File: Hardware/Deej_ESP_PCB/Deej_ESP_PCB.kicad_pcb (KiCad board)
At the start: 2 copper layers, 0 parts

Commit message: Started PCB Layout Added Mounting Holes and Knobs
- Started doing PCB layout. I have an idea of large component placement
  and therefore overall board size but still working out finalizing
  them.
- Added platted mounting holes to the board mostly for support since
  most of this board is user interfaces I expect there to be a good
  amount of force applied to the sliders, buttons, and knobs.
- Found some metal knobs for the rotary potentiometers and added them to
  the custom BOM.
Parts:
- added C1: 0.1uF, Capacitor_SMD:C_0603_1608Metric_Pad1.08x0.95mm_HandSolder, F.Cu at (-170.9, 104.7)
- added C10: 0.1uF, Capacitor_SMD:C_0603_1608Metric_Pad1.08x0.95mm_HandSolder, F.Cu at (-170.9, 112.2)
- added C11: 0.1uF, Capacitor_SMD:C_0603_1608Metric_Pad1.08x0.95mm_HandSolder, F.Cu at (-170.9, 114.7)
- added C12: 0.1uF, Capacitor_SMD:C_0603_1608Metric_Pad1.08x0.95mm_HandSolder, F.Cu at (-170.9, 117.2)
- added C13: 0.1uF, Capacitor_SMD:C_0603_1608Metric_Pad1.08x0.95mm_HandSolder, F.Cu at (-170.9, 119.7)
- added C14: 0.1uF, Capacitor_SMD:C_0603_1608Metric_Pad1.08x0.95mm_HandSolder, F.Cu at (-170.9, 122.2)
- added C15: 0.1uF, Capacitor_SMD:C_0603_1608Metric_Pad1.08x0.95mm_HandSolder, F.Cu at (-170.9, 124.7)
- added C16: 10uF, Capacitor_SMD:C_0603_1608Metric_Pad1.08x0.95mm_HandSolder, F.Cu at (-170.9, 127.2)
- added C17: 0.1uF, Capacitor_Tantalum_SMD:CP_EIA-3216-18_Kemet-A_HandSolder, F.Cu at (-123.7, 105.0)
- added C18: 0.1uF, Capacitor_Tantalum_SMD:CP_EIA-3216-18_Kemet-A_HandSolder, F.Cu at (-123.7, 108.1)
- added C19: 0.1uF, Capacitor_Tantalum_SMD:CP_EIA-3216-18_Kemet-A_HandSolder, F.Cu at (-123.7, 111.3)
- added C2: 0.1uF, Capacitor_SMD:C_0603_1608Metric_Pad1.08x0.95mm_HandSolder, F.Cu at (-170.9, 107.2)
- added C20: 0.1uF, Capacitor_Tantalum_SMD:CP_EIA-3216-18_Kemet-A_HandSolder, F.Cu at (-123.7, 114.4)
- added C21: 0.1uF, Capacitor_SMD:C_0603_1608Metric_Pad1.08x0.95mm_HandSolder, F.Cu at (-170.9, 129.8)
- added C22: 0.1uF, Capacitor_SMD:C_0603_1608Metric_Pad1.08x0.95mm_HandSolder, F.Cu at (-166.5, 104.7)
- added C23: 10uF, Capacitor_SMD:C_0603_1608Metric_Pad1.08x0.95mm_HandSolder, F.Cu at (-166.5, 107.2)
- added C24: 0.1uF, Capacitor_SMD:C_0603_1608Metric_Pad1.08x0.95mm_HandSolder, F.Cu at (-166.5, 109.7)
- added C25: 0.1uF, Capacitor_SMD:C_0603_1608Metric_Pad1.08x0.95mm_HandSolder, F.Cu at (-166.5, 112.2)
- added C26: 0.1uF, Capacitor_SMD:C_0603_1608Metric_Pad1.08x0.95mm_HandSolder, F.Cu at (-166.5, 114.7)
- added C27: 0.1uF, Capacitor_SMD:C_0603_1608Metric_Pad1.08x0.95mm_HandSolder, F.Cu at (-166.5, 117.2)
- added C28: 0.1uF, Capacitor_SMD:C_0603_1608Metric_Pad1.08x0.95mm_HandSolder, F.Cu at (-166.5, 119.7)
- added C29: 0.1uF, Capacitor_SMD:C_0603_1608Metric_Pad1.08x0.95mm_HandSolder, F.Cu at (-166.5, 122.2)
- added C3: 0.1uF, Capacitor_Tantalum_SMD:CP_EIA-3216-18_Kemet-A_HandSolder, F.Cu at (-129.7, 105.0)
- added C30: 1uF, Capacitor_SMD:C_0603_1608Metric_Pad1.08x0.95mm_HandSolder, F.Cu at (-166.5, 124.7)
- added C31: 0.1uF, Capacitor_Tantalum_SMD:CP_EIA-3216-18_Kemet-A_HandSolder, F.Cu at (-123.7, 117.6)
- added C32: 0.1uF, Capacitor_Tantalum_SMD:CP_EIA-3216-18_Kemet-A_HandSolder, F.Cu at (-123.7, 120.7)
- added C33: 0.1uF, Capacitor_Tantalum_SMD:CP_EIA-3216-18_Kemet-A_HandSolder, F.Cu at (-117.6, 105.0)
- added C34: 0.1uF, Capacitor_Tantalum_SMD:CP_EIA-3216-18_Kemet-A_HandSolder, F.Cu at (-117.6, 108.1)
- added C35: 0.1uF, Capacitor_Tantalum_SMD:CP_EIA-3216-18_Kemet-A_HandSolder, F.Cu at (-117.6, 111.3)
- added C36: 0.1uF, Capacitor_Tantalum_SMD:CP_EIA-3216-18_Kemet-A_HandSolder, F.Cu at (-117.6, 114.4)
- added C37: 22uF, Capacitor_SMD:C_0603_1608Metric_Pad1.08x0.95mm_HandSolder, F.Cu at (-166.5, 127.2)
- added C38: 0.1uF, Capacitor_SMD:C_0603_1608Metric_Pad1.08x0.95mm_HandSolder, F.Cu at (-166.5, 129.8)
- added C4: 0.1uF, Capacitor_Tantalum_SMD:CP_EIA-3216-18_Kemet-A_HandSolder, F.Cu at (-129.7, 108.1)
- added C5: 0.1uF, Capacitor_Tantalum_SMD:CP_EIA-3216-18_Kemet-A_HandSolder, F.Cu at (-129.7, 111.3)
- added C6: 0.1uF, Capacitor_Tantalum_SMD:CP_EIA-3216-18_Kemet-A_HandSolder, F.Cu at (-129.7, 114.4)
- added C7: 0.1uF, Capacitor_Tantalum_SMD:CP_EIA-3216-18_Kemet-A_HandSolder, F.Cu at (-129.7, 117.6)
- added C8: 0.1uF, Capacitor_Tantalum_SMD:CP_EIA-3216-18_Kemet-A_HandSolder, F.Cu at (-129.7, 120.7)
- added C9: 0.1uF, Capacitor_SMD:C_0603_1608Metric_Pad1.08x0.95mm_HandSolder, F.Cu at (-170.9, 109.7)
- added CR1: ESDALC6V1-1U2, STM:DIODE_ESDALC6V1-1U2_STM, F.Cu at (-111.8, 47.1)
- added CR10: ESDALC6V1-1U2, STM:DIODE_ESDALC6V1-1U2_STM, F.Cu at (-107.1, 47.1)
- added CR11: ESDALC6V1-1U2, STM:DIODE_ESDALC6V1-1U2_STM, F.Cu at (-107.1, 49.1)
- added CR12: ESDALC6V1-1U2, STM:DIODE_ESDALC6V1-1U2_STM, F.Cu at (-107.1, 51.2)
- added CR13: ESDALC6V1-1U2, STM:DIODE_ESDALC6V1-1U2_STM, F.Cu at (-107.1, 53.2)
- added CR14: ESDALC6V1-1U2, STM:DIODE_ESDALC6V1-1U2_STM, F.Cu at (-104.8, 47.1)
- added CR15: ESDALC6V1-1U2, STM:DIODE_ESDALC6V1-1U2_STM, F.Cu at (-104.8, 49.1)
- added CR16: ESDALC6V1-1U2, STM:DIODE_ESDALC6V1-1U2_STM, F.Cu at (-104.8, 51.2)
- added CR17: ESDALC6V1-1U2, STM:DIODE_ESDALC6V1-1U2_STM, F.Cu at (-104.8, 53.2)
- added CR2: ESDALC6V1-1U2, STM:DIODE_ESDALC6V1-1U2_STM, F.Cu at (-111.8, 49.1)
- added CR3: ESDALC6V1-1U2, STM:DIODE_ESDALC6V1-1U2_STM, F.Cu at (-111.8, 51.2)
- added CR4: ESDALC6V1-1U2, STM:DIODE_ESDALC6V1-1U2_STM, F.Cu at (-111.8, 53.2)
- added CR5: ESDALC6V1-1U2, STM:DIODE_ESDALC6V1-1U2_STM, F.Cu at (-109.5, 47.1)
- added CR6: ESDALC6V1-1U2, STM:DIODE_ESDALC6V1-1U2_STM, F.Cu at (-109.5, 49.1)
- added CR7: ESDA25P35-1U1M, STM:QFN1610_STM, F.Cu at (-101.3, 67.7)
- added CR8: ESDALC6V1-1U2, STM:DIODE_ESDALC6V1-1U2_STM, F.Cu at (-109.5, 51.2)
- added CR9: ESDALC6V1-1U2, STM:DIODE_ESDALC6V1-1U2_STM, F.Cu at (-109.5, 53.2)
- added D1: Inolux_IN-PI554FCH, LED_SMD:LED_Inolux_IN-PI554FCH_PLCC4_5.0x5.0mm_P3.2mm, F.Cu at (284.6, 151.7)
- added D10: Inolux_IN-PI554FCH, LED_SMD:LED_Inolux_IN-PI554FCH_PLCC4_5.0x5.0mm_P3.2mm, F.Cu at (148.0, 217.5)
- added D11: Inolux_IN-PI554FCH, LED_SMD:LED_Inolux_IN-PI554FCH_PLCC4_5.0x5.0mm_P3.2mm, F.Cu at (155.5, 217.5)
- added D12: Inolux_IN-PI554FCH, LED_SMD:LED_Inolux_IN-PI554FCH_PLCC4_5.0x5.0mm_P3.2mm, F.Cu at (174.5, 217.5)
- added D13: Red LED, LED_SMD:LED_0603_1608Metric_Pad1.05x0.95mm_HandSolder, F.Cu at (-100.3, 55.5)
- added D14: Inolux_IN-PI554FCH, LED_SMD:LED_Inolux_IN-PI554FCH_PLCC4_5.0x5.0mm_P3.2mm, F.Cu at (182.0, 217.5)
- added D15: Inolux_IN-PI554FCH, LED_SMD:LED_Inolux_IN-PI554FCH_PLCC4_5.0x5.0mm_P3.2mm, F.Cu at (201.0, 217.5)
- added D16: Inolux_IN-PI554FCH, LED_SMD:LED_Inolux_IN-PI554FCH_PLCC4_5.0x5.0mm_P3.2mm, F.Cu at (208.5, 217.5)
- added D17: Inolux_IN-PI554FCH, LED_SMD:LED_Inolux_IN-PI554FCH_PLCC4_5.0x5.0mm_P3.2mm, F.Cu at (227.5, 217.5)
- added D18: MMSD4148T1G, Diode_SMD:D_SOD-123, F.Cu at (-110.0, 69.3)
- added D19: MMSD4148T1G, Diode_SMD:D_SOD-123, F.Cu at (-110.0, 72.6)
- added D2: Inolux_IN-PI554FCH, LED_SMD:LED_Inolux_IN-PI554FCH_PLCC4_5.0x5.0mm_P3.2mm, F.Cu at (284.6, 232.0)
- added D20: MMSD4148T1G, Diode_SMD:D_SOD-123, F.Cu at (-110.0, 76.0)
- added D21: MMSD4148T1G, Diode_SMD:D_SOD-123, F.Cu at (-110.0, 79.3)
- added D22: Orange LED, LED_SMD:LED_0603_1608Metric_Pad1.05x0.95mm_HandSolder, F.Cu at (-100.3, 58.1)
- added D23: Inolux_IN-PI554FCH, LED_SMD:LED_Inolux_IN-PI554FCH_PLCC4_5.0x5.0mm_P3.2mm, F.Cu at (235.0, 217.5)
- added D24: Inolux_IN-PI554FCH, LED_SMD:LED_Inolux_IN-PI554FCH_PLCC4_5.0x5.0mm_P3.2mm, F.Cu at (254.0, 217.5)
- added D25: Orange LED, LED_SMD:LED_0603_1608Metric_Pad1.05x0.95mm_HandSolder, F.Cu at (-100.3, 60.7)
- added D26: Green LED, LED_SMD:LED_0603_1608Metric_Pad1.05x0.95mm_HandSolder, F.Cu at (-100.3, 63.2)
- added D3: Inolux_IN-PI554FCH, LED_SMD:LED_Inolux_IN-PI554FCH_PLCC4_5.0x5.0mm_P3.2mm, F.Cu at (102.5, 217.5)
- added D4: Inolux_IN-PI554FCH, LED_SMD:LED_Inolux_IN-PI554FCH_PLCC4_5.0x5.0mm_P3.2mm, F.Cu at (121.5, 217.5)
- added D5: MMSD4148T1G, Diode_SMD:D_SOD-123, F.Cu at (-110.0, 55.9)
- added D6: MMSD4148T1G, Diode_SMD:D_SOD-123, F.Cu at (-110.0, 59.2)
- added D7: MMSD4148T1G, Diode_SMD:D_SOD-123, F.Cu at (-110.0, 62.6)
- added D8: MMSD4148T1G, Diode_SMD:D_SOD-123, F.Cu at (-110.0, 65.9)
- added D9: Inolux_IN-PI554FCH, LED_SMD:LED_Inolux_IN-PI554FCH_PLCC4_5.0x5.0mm_P3.2mm, F.Cu at (129.0, 217.5)
- added H1: ~, MountingHole:MountingHole_3.2mm_M3_Pad, F.Cu at (101.0, 62.5)
- added H10: MountingHole_Pad, MountingHole:MountingHole_3.2mm_M3_Pad, F.Cu at (125.5, 155.0)
- added H11: MountingHole_Pad, MountingHole:MountingHole_3.2mm_M3_Pad, F.Cu at (178.5, 155.0)
- added H12: MountingHole_Pad, MountingHole:MountingHole_3.2mm_M3_Pad, F.Cu at (231.5, 155.0)
- added H2: ~, MountingHole:MountingHole_3.2mm_M3_Pad, F.Cu at (101.0, 238.0)
- added H3: ~, MountingHole:MountingHole_3.2mm_M3_Pad, F.Cu at (151.5, 238.0)
- added H4: ~, MountingHole:MountingHole_3.2mm_M3_Pad, F.Cu at (204.5, 238.0)
- added H5: ~, MountingHole:MountingHole_3.2mm_M3_Pad, F.Cu at (257.5, 238.0)
- added H6: MountingHole_Pad, MountingHole:MountingHole_3.2mm_M3_Pad, F.Cu at (299.0, 238.0)
- added H7: MountingHole_Pad, MountingHole:MountingHole_3.2mm_M3_Pad, F.Cu at (299.0, 157.0)
- added H8: MountingHole_Pad, MountingHole:MountingHole_3.2mm_M3_Pad, F.Cu at (299.0, 62.5)
- added H9: MountingHole_Pad, MountingHole:MountingHole_3.2mm_M3_Pad, F.Cu at (190.0, 62.5)
- added J1: USB_C_Receptacle_USB2.0_16P, Connector_USB:USB_C_Receptacle_GCT_USB4085, F.Cu at (182.0, 64.5)
- added J2: UART Header, Connector_PinHeader_2.54mm:PinHeader_1x04_P2.54mm_Vertical, F.Cu at (262.3, 91.5)
- added P1: 10K, Bourns_Potentiometer:PTL0115R0103B1, F.Cu at (113.2, 93.5)
- added P2: 10K, Bourns_Potentiometer:PTL0115R0103B1, F.Cu at (139.8, 93.5)
- added P3: 10K, Bourns_Potentiometer:PTL0115R0103B1, F.Cu at (166.2, 93.5)
- added P4: 10K, Bourns_Potentiometer:PTL0115R0103B1, F.Cu at (192.8, 93.5)
- added P5: 10K, Bourns_Potentiometer:PTL0115R0103B1, F.Cu at (219.2, 93.5)
- added P6: 10K, Bourns_Potentiometer:PTL0115R0103B1, F.Cu at (245.8, 93.5)
- added R1: 499, Capacitor_SMD:C_0603_1608Metric_Pad1.08x0.95mm_HandSolder, F.Cu at (-162.2, 104.7)
- added R10: 5.1K, Capacitor_SMD:C_0603_1608Metric_Pad1.08x0.95mm_HandSolder, F.Cu at (-162.2, 127.2)
- added R11: 5.1K, Capacitor_SMD:C_0603_1608Metric_Pad1.08x0.95mm_HandSolder, F.Cu at (-162.2, 129.8)
- added R12: 200, Capacitor_SMD:C_0603_1608Metric_Pad1.08x0.95mm_HandSolder, F.Cu at (-157.8, 104.7)
- added R13: 1K, Capacitor_SMD:C_0603_1608Metric_Pad1.08x0.95mm_HandSolder, F.Cu at (-157.8, 107.2)
- added R14: 1K, Capacitor_SMD:C_0603_1608Metric_Pad1.08x0.95mm_HandSolder, F.Cu at (-157.8, 109.7)
- added R15: 1K, Capacitor_SMD:C_0603_1608Metric_Pad1.08x0.95mm_HandSolder, F.Cu at (-157.8, 112.2)
- added R16: 1K, Capacitor_SMD:C_0603_1608Metric_Pad1.08x0.95mm_HandSolder, F.Cu at (-157.8, 114.7)
- added R17: 10K, Capacitor_SMD:C_0603_1608Metric_Pad1.08x0.95mm_HandSolder, F.Cu at (-157.8, 117.2)
- added R18: 10K, Capacitor_SMD:C_0603_1608Metric_Pad1.08x0.95mm_HandSolder, F.Cu at (-157.8, 119.7)
- added R19: 10K, Capacitor_SMD:C_0603_1608Metric_Pad1.08x0.95mm_HandSolder, F.Cu at (-157.8, 122.2)
- added R2: 1K, Capacitor_SMD:C_0603_1608Metric_Pad1.08x0.95mm_HandSolder, F.Cu at (-162.2, 107.2)
- added R20: 10K, Capacitor_SMD:C_0603_1608Metric_Pad1.08x0.95mm_HandSolder, F.Cu at (-157.8, 124.7)
- added R21: 100, Capacitor_SMD:C_0603_1608Metric_Pad1.08x0.95mm_HandSolder, F.Cu at (-157.8, 127.2)
- added R23: 100, Capacitor_SMD:C_0603_1608Metric_Pad1.08x0.95mm_HandSolder, F.Cu at (-157.8, 129.8)
- added R24: 10, Capacitor_SMD:C_0603_1608Metric_Pad1.08x0.95mm_HandSolder, F.Cu at (-153.5, 104.7)
- added R25: 10K, Capacitor_SMD:C_0603_1608Metric_Pad1.08x0.95mm_HandSolder, F.Cu at (-153.5, 107.2)
- added R26: 100, Capacitor_SMD:C_0603_1608Metric_Pad1.08x0.95mm_HandSolder, F.Cu at (-153.5, 109.7)
- added R27: 100, Capacitor_SMD:C_0603_1608Metric_Pad1.08x0.95mm_HandSolder, F.Cu at (-153.5, 112.2)
- added R28: 100, Capacitor_SMD:C_0603_1608Metric_Pad1.08x0.95mm_HandSolder, F.Cu at (-153.5, 114.7)
- added R29: 100, Capacitor_SMD:C_0603_1608Metric_Pad1.08x0.95mm_HandSolder, F.Cu at (-153.5, 117.2)
- added R3: 1K, Capacitor_SMD:C_0603_1608Metric_Pad1.08x0.95mm_HandSolder, F.Cu at (-162.2, 109.7)
- added R30: 100, Capacitor_SMD:C_0603_1608Metric_Pad1.08x0.95mm_HandSolder, F.Cu at (-153.5, 119.7)
- added R31: 100, Capacitor_SMD:C_0603_1608Metric_Pad1.08x0.95mm_HandSolder, F.Cu at (-153.5, 122.2)
- added R4: 1K, Capacitor_SMD:C_0603_1608Metric_Pad1.08x0.95mm_HandSolder, F.Cu at (-162.2, 112.2)
- added R5: 1K, Capacitor_SMD:C_0603_1608Metric_Pad1.08x0.95mm_HandSolder, F.Cu at (-162.2, 114.7)
- added R6: 10K, Capacitor_SMD:C_0603_1608Metric_Pad1.08x0.95mm_HandSolder, F.Cu at (-162.2, 117.2)
- added R7: 10K, Capacitor_SMD:C_0603_1608Metric_Pad1.08x0.95mm_HandSolder, F.Cu at (-162.2, 119.7)
- added R8: 10K, Capacitor_SMD:C_0603_1608Metric_Pad1.08x0.95mm_HandSolder, F.Cu at (-162.2, 122.2)
- added R9: 10K, Capacitor_SMD:C_0603_1608Metric_Pad1.08x0.95mm_HandSolder, F.Cu at (-162.2, 124.7)
- added SW1: SW_Push, PCM_Switch_Keyboard_Cherry_MX:SW_Cherry_MX_PCB, F.Cu at (112.0, 234.0)
- added SW2: SW_Push, PCM_Switch_Keyboard_Cherry_MX:SW_Cherry_MX_PCB, F.Cu at (138.5, 234.0)
- added SW3: SW_Push, PCM_Switch_Keyboard_Cherry_MX:SW_Cherry_MX_PCB, F.Cu at (165.0, 234.0)
- added SW4: SW_Push, PCM_Switch_Keyboard_Cherry_MX:SW_Cherry_MX_PCB, F.Cu at (191.5, 234.0)
- added SW5: SW_Push, PCM_Switch_Keyboard_Cherry_MX:SW_Cherry_MX_PCB, F.Cu at (218.0, 234.0)
- added SW6: SW_Push, PCM_Switch_Keyboard_Cherry_MX:SW_Cherry_MX_PCB, F.Cu at (244.5, 234.0)
- added SW7: Reset, TEConnectivity:SWITCH_FSMSM_TYC, F.Cu at (282.0, 69.0)
- added U1: 10K, Bourns_Potentiometer:39LA-1PB-103, F.Cu at (284.5, 140.7)
- added U10: 1.3" 128x64 OLED, Adafruit:Adafruit_1_3_OLED, F.Cu at (129.6, 62.8)
- added U11: 1.3" 128x64 OLED, Adafruit:Adafruit_1_3_OLED, F.Cu at (208.6, 62.8)
- added U2: 10K, Bourns_Potentiometer:39LA-1PB-103, F.Cu at (284.6, 221.0)
- added U3: ECMF02-2AMX6, STM:QFN-6L_STM, F.Cu at (179.0, 67.5)
- added U4: SN74HCS126DR, TI:D0014A-IPC_A, F.Cu at (260.0, 203.0)
- added U5: LMS1585ACS-3.3/NOPB, TI:KTT0003B, F.Cu at (177.5, 80.0)
- added U6: SN74HCS126DR, TI:D0014A-IPC_A, F.Cu at (151.5, 227.0)
- added U7: ESP32-S3-MINI-1U, ESP32:ESP32S3MINI1UN8, F.Cu at (258.0, 71.5)
- added U8: 1.3" 128x64 OLED, Adafruit:Adafruit_1_3_OLED, F.Cu at (275.6, 88.0)
- added U9: 1.3" 128x64 OLED, Adafruit:Adafruit_1_3_OLED, F.Cu at (275.6, 168.5)
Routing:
- added copper zone on B.Cu, net GND
- added copper zone on F.Cu, net GND
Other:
- board outline added: 206 x 183.5 mm

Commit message: All Components Placed and OSH Park Rules Set.
- I have placed all of the components and I am looking at starting trace
  layout.
- I have also set the rules and board stack up specifications for OSH
  Park to ensure thaat the design is as similr to how the final product
  will be.
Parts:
- C17, C18, C19, C20, C7, C8, CR10, CR11, CR5, CR6, CR8, CR9, D18, D19, D20, D21, D7, D8, R13, R14, R15, R16, R17, R18, R19, R20, R4, R5, R8, R9: moved to B.Cu
- moved C9 472.6 mm to (284.5, 236.0), turned to 180 degrees
- moved C1 458.2 mm to (284.5, 155.5), turned to 180 degrees
- moved R3 452.8 mm to (276.5, 222.0), turned to -90 degrees
- moved R7 449.7 mm to (276.5, 218.5), turned to -90 degrees
- moved R1 444.7 mm to (280.0, 152.5), turned to -90 degrees
- moved C29 441.1 mm to (270.4, 61.2)
- moved R2 439.5 mm to (276.0, 141.5), turned to -90 degrees
- moved R6 438.7 mm to (276.0, 138.0), turned to -90 degrees
- moved C13 436.4 mm to (258.5, 197.5), turned to 180 degrees
- moved C5 434.7 mm to (292.0, 216.5), turned to -60 degrees
- moved C30 434.6 mm to (264.6, 69.5), turned to -90 degrees
- moved C28 432.7 mm to (254.0, 221.5), turned to 180 degrees
- moved R8 428.8 mm to (253.5, 227.5), turned to -90 degrees
- moved R4 428.2 mm to (249.5, 230.0), turned to -90 degrees
- moved CR2 426.5 mm to (282.0, 213.0), turned to -160 degrees
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- renumbered H11 to H10, H6 to H11, H7 to H2, H2 to H3, H8 to H4, H3 to H5, H9 to H6, H4 to H7, H10 to H8, H5 to H9, R23 to R22, R24 to R23, R25 to R24, R26 to R25, R27 to R26, R28 to R27, R29 to R28, R30 to R29, R31 to R30, SW6 to SW1, SW5 to SW2, SW1 to SW3, SW2 to SW4, SW3 to SW5, SW4 to SW6
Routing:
- net +5V: track 0.00 -> 345.0 mm, vias 0 -> 20
- net +3.3V: track 0.00 -> 81.4 mm
- net /UART_RX: track 0.00 -> 13.6 mm
- net /UART_TX: track 0.00 -> 13.5 mm
- net Net-(U7-EN): track 0.00 -> 13.4 mm
- net GND: track 0.00 -> 12.5 mm
- net Net-(D7-K): track 0.00 -> 7.49 mm
- net Net-(D8-K): track 0.00 -> 7.36 mm
- net Net-(D21-K): track 0.00 -> 7.36 mm
- net Net-(D19-K): track 0.00 -> 7.36 mm
- net Net-(D20-K): track 0.00 -> 7.17 mm
- net Net-(D8-A): track 0.00 -> 7.08 mm
- net Net-(D21-A): track 0.00 -> 7.08 mm
- net Net-(D20-A): track 0.00 -> 6.90 mm
- net Net-(D7-A): track 0.00 -> 6.88 mm
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- added copper zone on B.Cu, net +5V
- added copper zone on F.Cu, net +5V
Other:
- rule pad_to_mask_clearance: 0 -> 0.0508

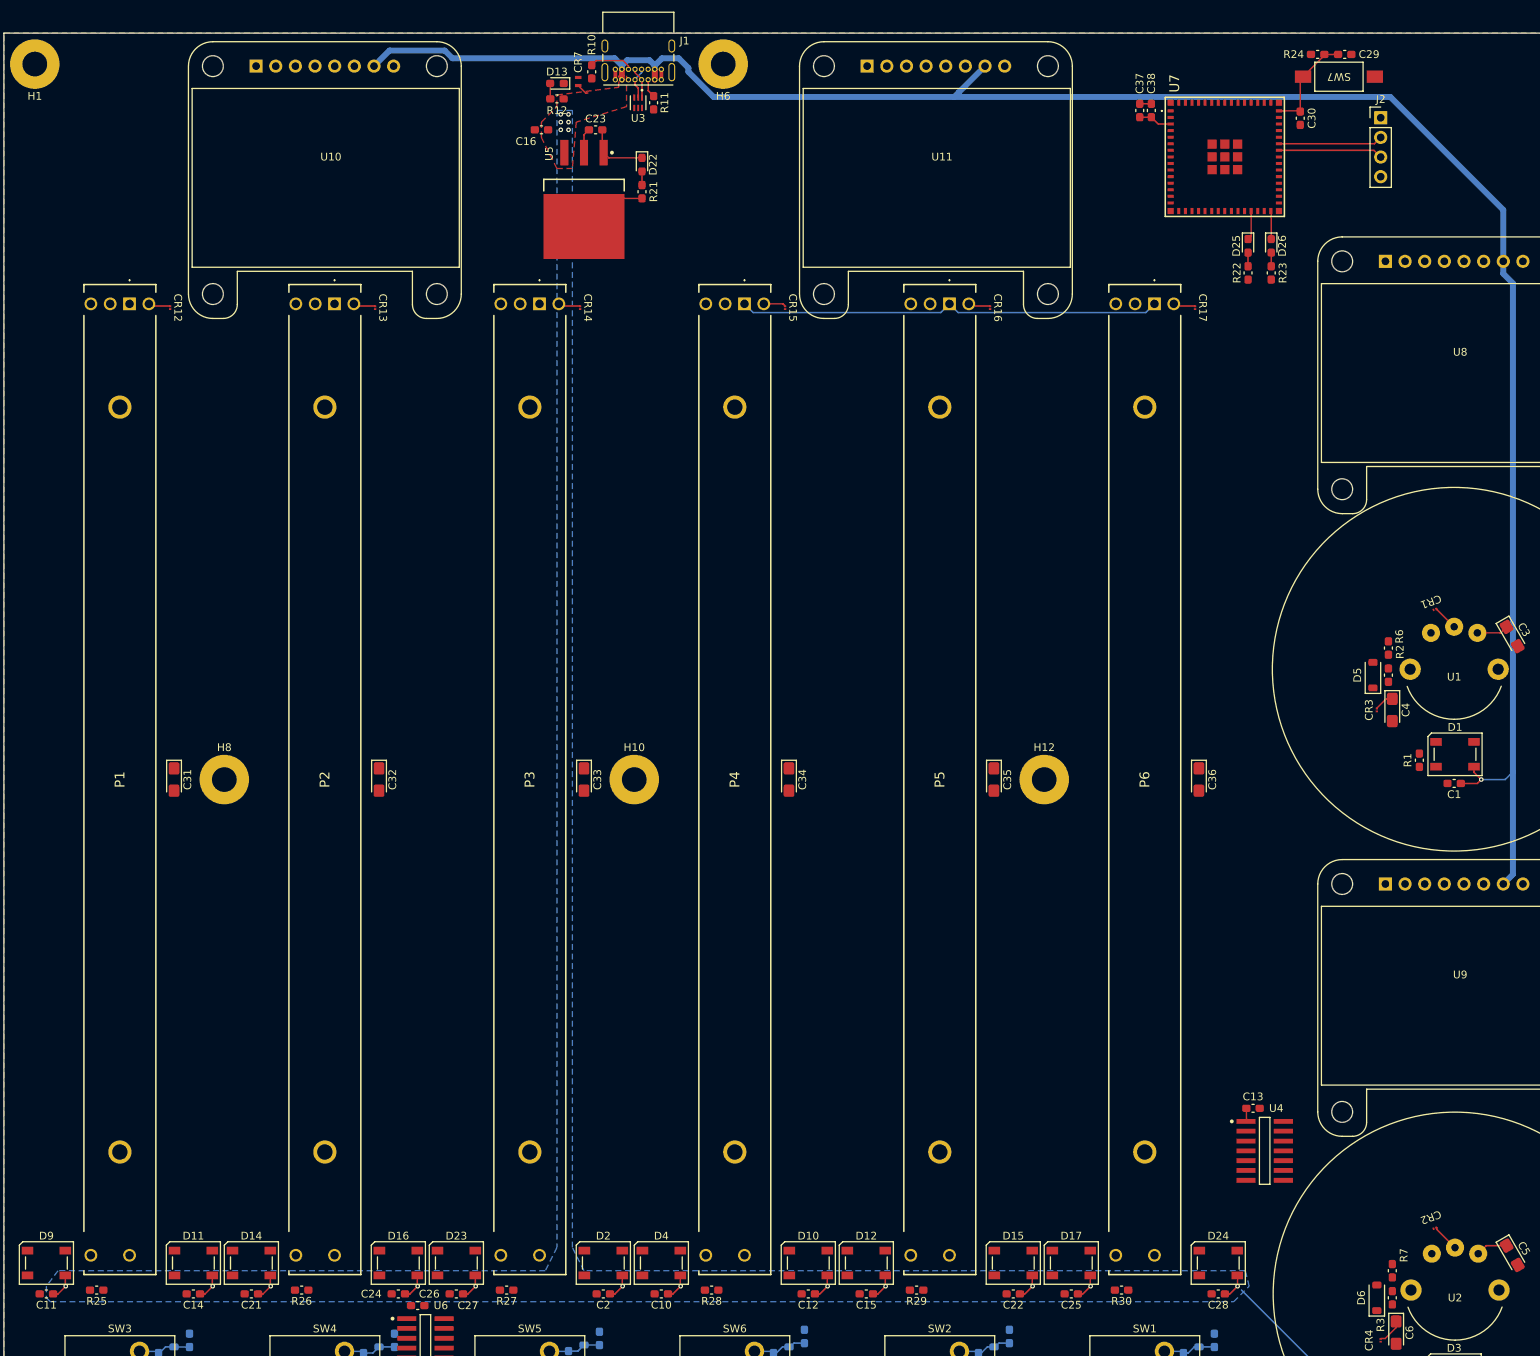
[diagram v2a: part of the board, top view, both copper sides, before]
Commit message: Getting Back into it
I had gotten a little more busy and wasn't able to get back to it.
- Routed some more power traces
- Routed the analog signals for the slide potentiometers
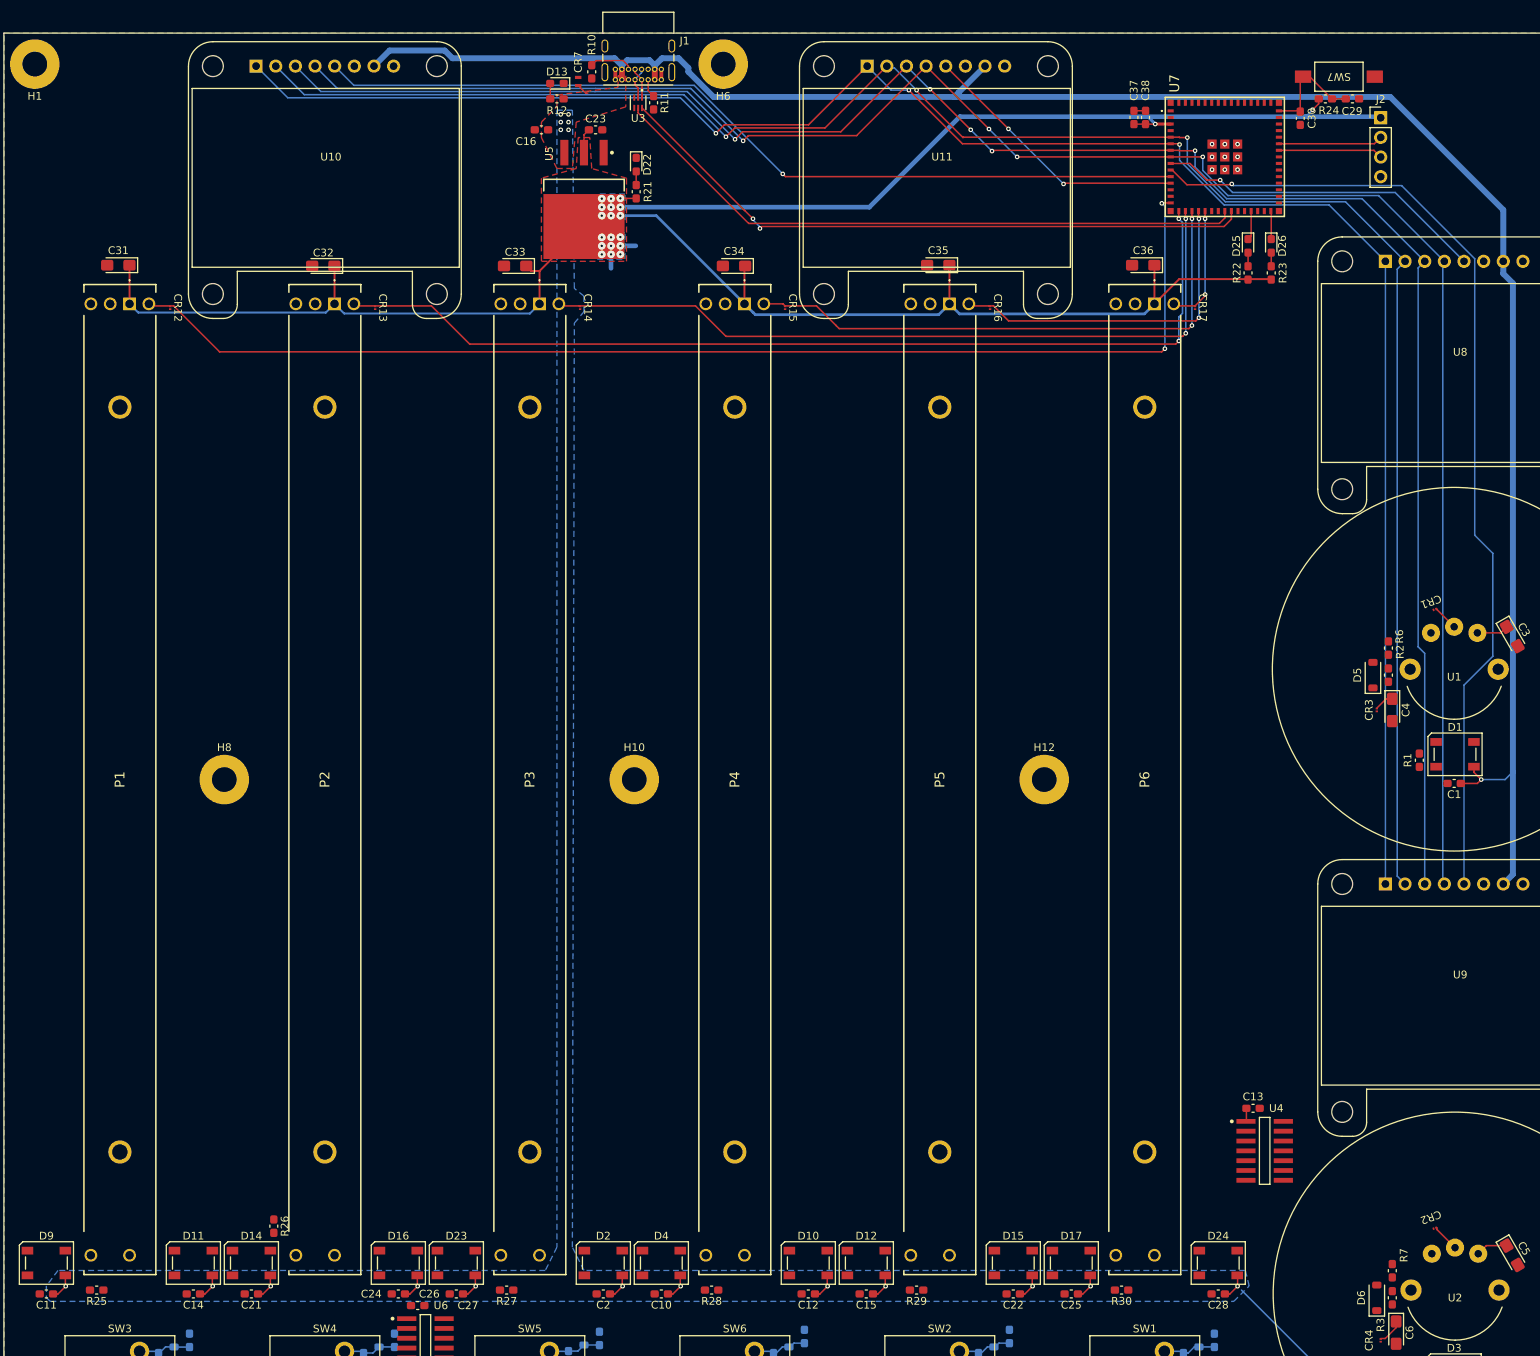
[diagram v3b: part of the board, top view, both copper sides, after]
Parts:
- moved C33 67.0 mm to (163.1, 88.6), turned to 180 degrees
- moved C31 66.9 mm to (111.8, 88.5), turned to 180 degrees
- moved C35 66.9 mm to (217.8, 88.5), turned to 180 degrees
- moved C36 66.9 mm to (244.3, 88.5), turned to 180 degrees
- moved C32 66.8 mm to (138.3, 88.6), turned to 180 degrees
- moved C34 66.8 mm to (191.4, 88.6), turned to 180 degrees
- moved R26 9.01 mm to (131.9, 212.7), turned to -90 degrees
- moved C29 5.84 mm to (271.4, 67.0)
- moved R24 5.84 mm to (267.9, 67.0)
- moved C37 1.17 mm to (243.1, 69.4)
- moved C38 1.17 mm to (244.6, 69.4)
- moved D22 0.75 mm to (178.8, 75.5)
- moved R21 0.75 mm to (178.8, 79.0)
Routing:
- net /SCLK: track 0.00 -> 247.5 mm, vias 0 -> 3
- net /D/C: track 0.00 -> 246.8 mm, vias 0 -> 5
- net /RST: track 0.00 -> 246.1 mm, vias 0 -> 4
- net /MOSI: track 0.00 -> 245.3 mm, vias 0 -> 3
- net +3.3V: track 81.4 -> 324.0 mm, vias 0 -> 20
- net /Analog_2: track 2.86 -> 154.2 mm, vias 0 -> 2
- net /CS1: track 0.00 -> 127.5 mm, vias 0 -> 1
- net /Analog_3: track 2.86 -> 126.2 mm, vias 0 -> 2
- net /CS2: track 0.00 -> 114.0 mm, vias 0 -> 1
- net /Analog_4: track 2.86 -> 98.9 mm, vias 0 -> 2
- net /USB_D+: track 0.00 -> 84.4 mm, vias 0 -> 2
- net /USB_D-: track 0.00 -> 83.6 mm
- net /Analog_5: track 2.86 -> 71.6 mm, vias 0 -> 2
- net /CS0: track 0.00 -> 43.2 mm, vias 0 -> 1
- net /Analog_6: track 2.86 -> 44.7 mm, vias 0 -> 2
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- added copper zone on B.Cu, net +3.3V
- added copper zone on F.Cu, net +3.3V
